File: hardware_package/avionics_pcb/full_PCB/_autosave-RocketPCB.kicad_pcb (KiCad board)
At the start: 2 copper layers, 0.8 x 1 mm, 72 parts, among them J1 DX07S024XJ1R1100, J2 Micro_SD_Card, J3 Conn_01x03_Female, M1 Motor_Servo_JR, M2 Motor_Servo_JR, Q1 DMG2301L, Q2 DMG2301L, SW1 SW_Push, SW2 SW_Push, U1 STM32F405RGTx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

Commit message: Modified to 4 layer PCB, laid out 6V and 3V3 regulators
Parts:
- added R16: 4.7K, Resistor_SMD:R_0603_1608Metric, F.Cu at (188.5, 62.0)
- C7: value C -> 100nF
- moved SW2 17.4 mm to (130.3, 76.2), turned to 180 degrees
- moved SW1 8.84 mm to (139.7, 67.8), turned to 180 degrees
- moved C19 6.35 mm to (168.1, 74.7)
- moved C20 6.35 mm to (170.0, 74.7)
- moved C21 6.35 mm to (161.0, 74.7)
- moved C23 6.35 mm to (162.8, 74.7)
- moved C11 6.35 mm to (164.6, 74.7)
- moved C26 6.35 mm to (159.3, 74.7)
- moved C27 6.35 mm to (166.4, 74.7)
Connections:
- net /A0 renamed Net-(U1-Pad20)
- net /CLKIN renamed Net-(U4-Pad8)
- U1 pad 16: /PPS -> Net-(U1-Pad16)
- U1 pad 21: /INT2 -> Net-(U1-Pad21)
- U1 pad 22: /INT1 -> Net-(U1-Pad22)
- U1 pad 23: /INT -> Net-(U1-Pad23)
- U1 pad 26: /CS -> Net-(U1-Pad26)
- U3 pad 8: /CS -> Net-(R16-Pad2)
- U4 pad 6: /INT -> Net-(U4-Pad6)
- U7 pad 5: /INT2 -> Net-(U7-Pad5)
- U7 pad 6: /INT1 -> Net-(U7-Pad6)
- U8 pad 11: /PPS -> Net-(U8-Pad11)
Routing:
- net GND: track 139.4 -> 80.6 mm
- net +3V3: track 33.7 -> 36.9 mm
- added copper zone on PWR, net +3V3
- added copper zone on GND, net GND
- removed copper zone on B.Cu, net GND
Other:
- copper layers 2 -> 4

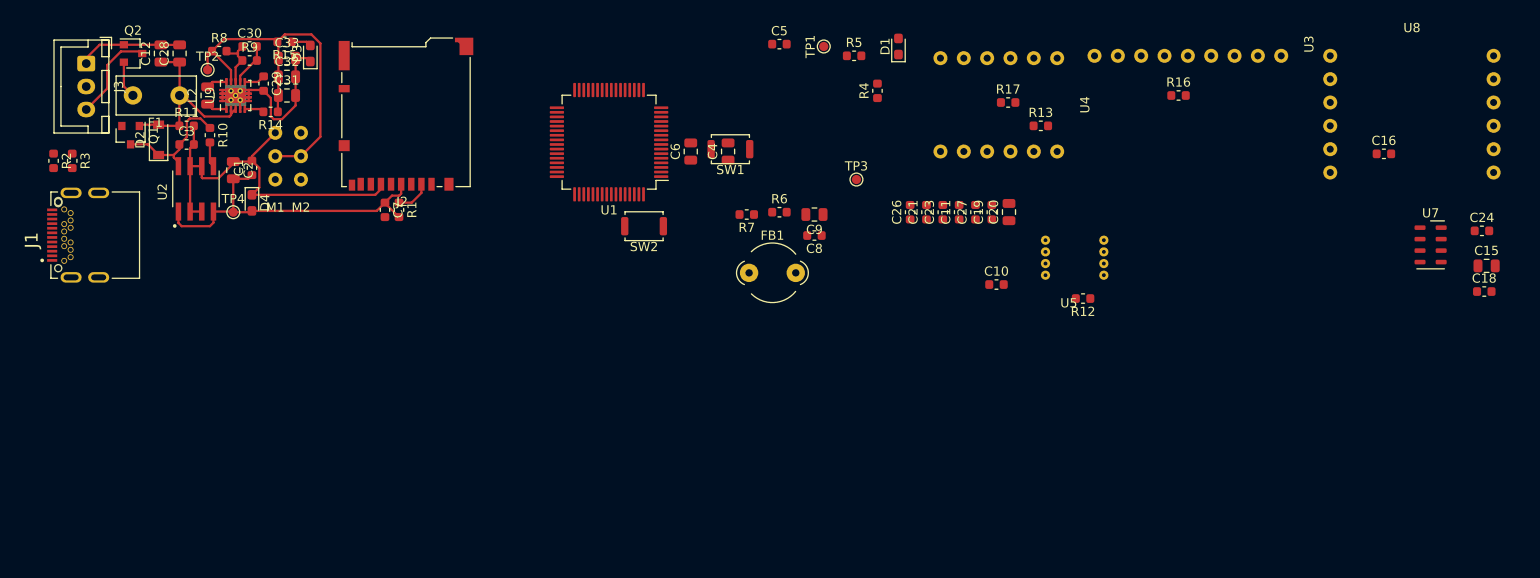
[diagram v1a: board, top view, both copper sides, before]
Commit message: Laid out and routed the majority of the board
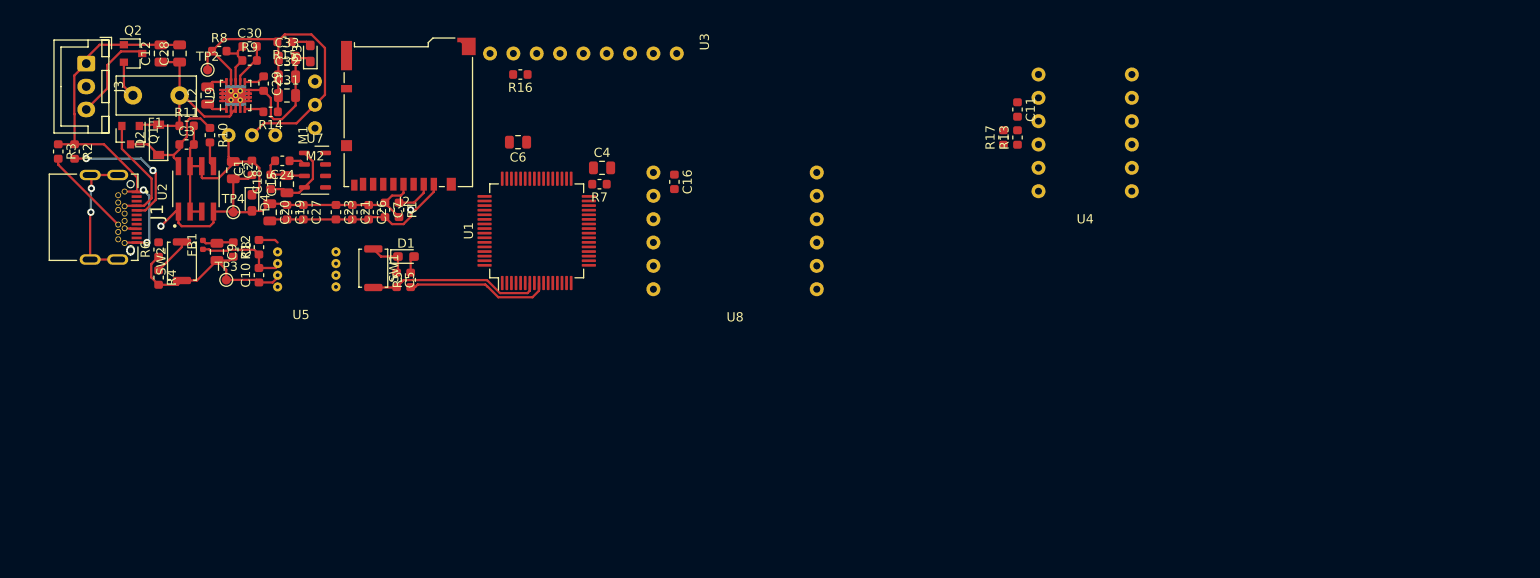
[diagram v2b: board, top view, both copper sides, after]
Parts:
- removed TP1: TestPoint, TestPoint:TestPoint_Pad_D1.0mm
- FB1: footprint Ferrite_THT:LairdTech_28C0236-0JW-10 -> Resistor_SMD:R_0402_1005Metric
- moved C18 132.6 mm to (89.7, 71.4), turned to 90 degrees
- moved C15 130.9 mm to (91.4, 71.6), turned to 90 degrees
- moved C24 130.8 mm to (90.9, 69.1), turned to 180 degrees
- moved U7 121.7 mm to (94.5, 70.1)
- moved R12 89.9 mm to (88.4, 78.5), turned to 90 degrees
- moved U5 83.6 mm to (93.0, 85.3)
- moved R4 80.8 mm to (77.5, 81.8), turned to 270 degrees
- moved C20 80.4 mm to (89.6, 74.7), turned to 270 degrees
- moved C10 80.3 mm to (88.4, 81.5), turned to 90 degrees
- moved U8 78.8 mm to (140.2, 84.3), turned to 0 degrees
- moved C16 77.3 mm to (133.6, 71.4), turned to 270 degrees
- moved C19 76.7 mm to (91.4, 74.7), turned to 270 degrees
- moved C27 73.2 mm to (93.2, 74.7), turned to 270 degrees
- moved R16 71.7 mm to (116.8, 59.7), turned to 180 degrees
- moved TP3 69.4 mm to (84.8, 82.0)
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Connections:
- U1 pad 39: /SDIO_D0 -> /SDIO_D1
- U1 pad 40: /SDIO_D1 -> /SDIO_D0
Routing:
- net GND: track 80.6 -> 149.4 mm, vias 0 -> 3
- net +3V3: track 36.9 -> 68.7 mm, vias 0 -> 1
- net ~RESET~: track 0.00 -> 18.9 mm
- net /D13: track 0.00 -> 15.8 mm
- net Net-(J1-PadS1): track 0.00 -> 15.3 mm, vias 0 -> 2
- net Net-(J1-PadA5): track 0.00 -> 15.0 mm, vias 0 -> 2
- net VBUS: track 0.00 -> 13.8 mm
- net Net-(J1-PadB5): track 0.00 -> 9.87 mm
- net /BOOT0: track 0.00 -> 4.14 mm
- net Net-(C8-Pad1): track 0.00 -> 3.47 mm
- net /FLASH_CS: track 0.00 -> 2.15 mm
- net Net-(D1-Pad2): track 0.00 -> 1.90 mm
- net Net-(C24-Pad1): track 0.00 -> 1.78 mm
